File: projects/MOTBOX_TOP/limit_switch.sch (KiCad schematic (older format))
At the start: 3 parts, among them J17 Conn_02x02_Top_Bottom, SW1 SW_SPST, SW2 SW_SPST

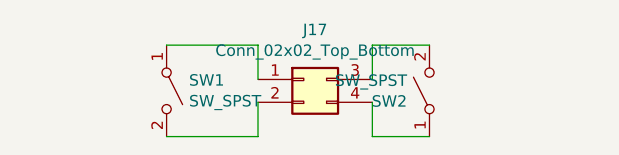
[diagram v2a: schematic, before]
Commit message: New library files and schematics with ESE31 and DT045 switches
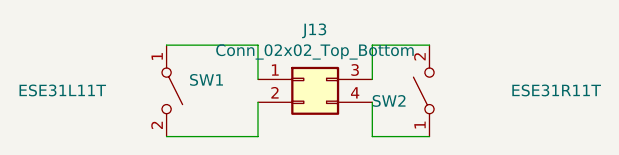
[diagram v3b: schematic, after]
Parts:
- SW1: value SW_SPST -> ESE31L11T
- SW2: value SW_SPST -> ESE31R11T
- renumbered J17 to J13
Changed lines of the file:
@@
 EESchema Schematic File Version 4
 LIBS:MOTBOX_TOP-cache
+LIBS:motbox_with_promini_v1_2-cache
 EELAYER 26 0
 EELAYER END
@@
 P 3050 2800
 F 0 "SW1" V 3004 2898 50  0000 L CNN
-F 1 "SW_SPST" V 3095 2898 50  0000 L CNN
+F 1 "ESE31L11T" V 3050 2150 50  0000 L CNN
 F 2 "mylib:Detector_SW_2pin_right" H 3050 2800 50  0001 C CNN
 F 3 "" H 3050 2800 50  0001 C CNN
@@
 P 4200 2800
 F 0 "SW2" V 4154 2898 50  0000 L CNN
-F 1 "SW_SPST" V 4245 2898 50  0000 L CNN
+F 1 "ESE31R11T" V 4200 2050 50  0000 L CNN
 F 2 "mylib:Detector_SW_2pin_left" H 4200 2800 50  0001 C CNN
 F 3 "" H 4200 2800 50  0001 C CNN
@@
 $EndComp
 $Comp
-L Connector_Generic:Conn_02x02_Top_Bottom J17
+L Connector_Generic:Conn_02x02_Top_Bottom J13
 U 1 1 5CC19B02
 P 3650 2750
-F 0 "J17" H 3700 2967 50  0000 C CNN
+F 0 "J13" H 3700 2967 50  0000 C CNN
 F 1 "Conn_02x02_Top_Bottom" H 3700 2876 50  0000 C CNN
 F 2 "Connector_Wire:SolderWirePad_2x02_P2.54mm_Drill0.8mm" H 3650 2750 50  0001 C CNN
